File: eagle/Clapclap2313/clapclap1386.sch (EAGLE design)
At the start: 26 parts, among them IC1 TINY13-20PU, J1 AVR_SPI_PRG_6PTH, K1 4052, M1 Mic, U1 LM386

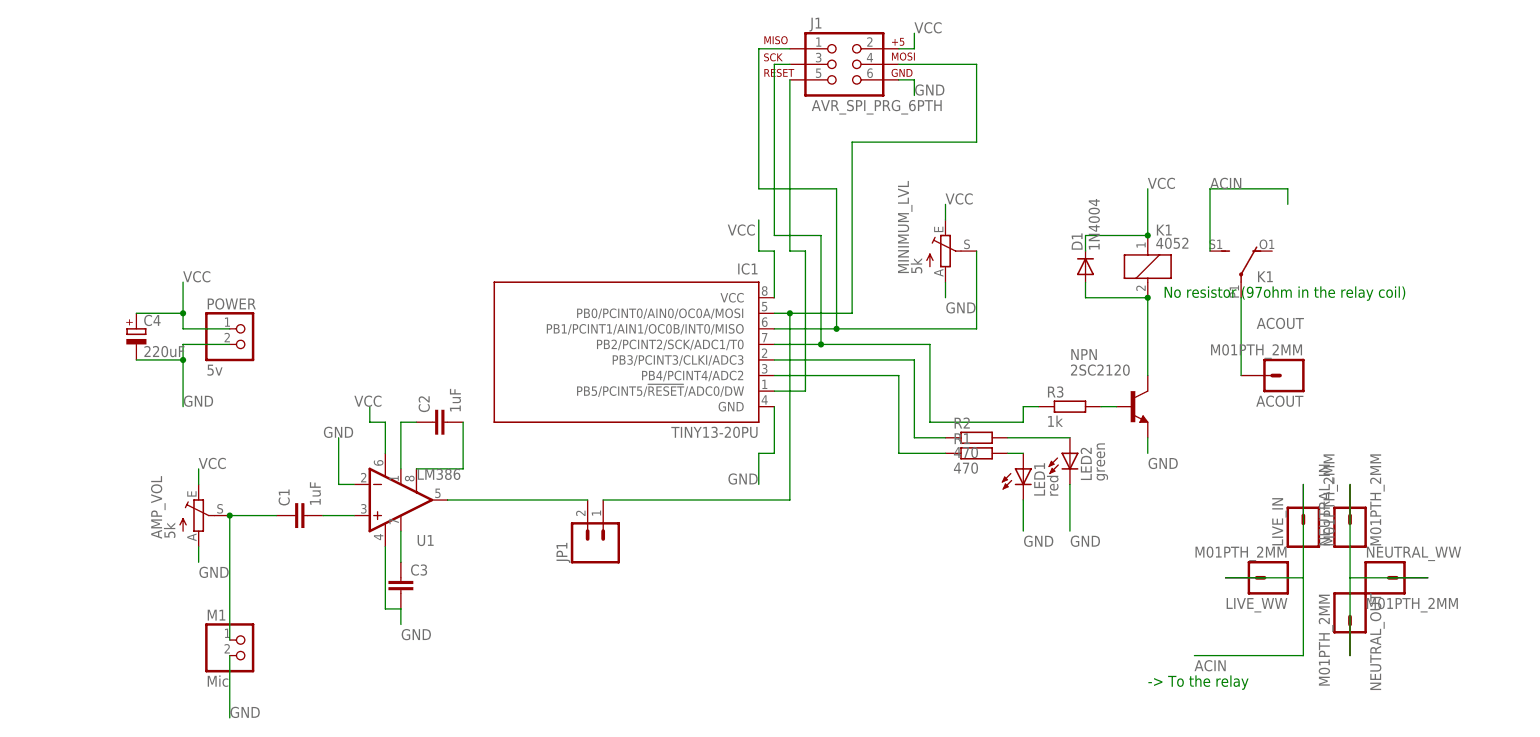
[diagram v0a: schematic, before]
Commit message: Clapclap 1386 Beta version : needs holes and full verification
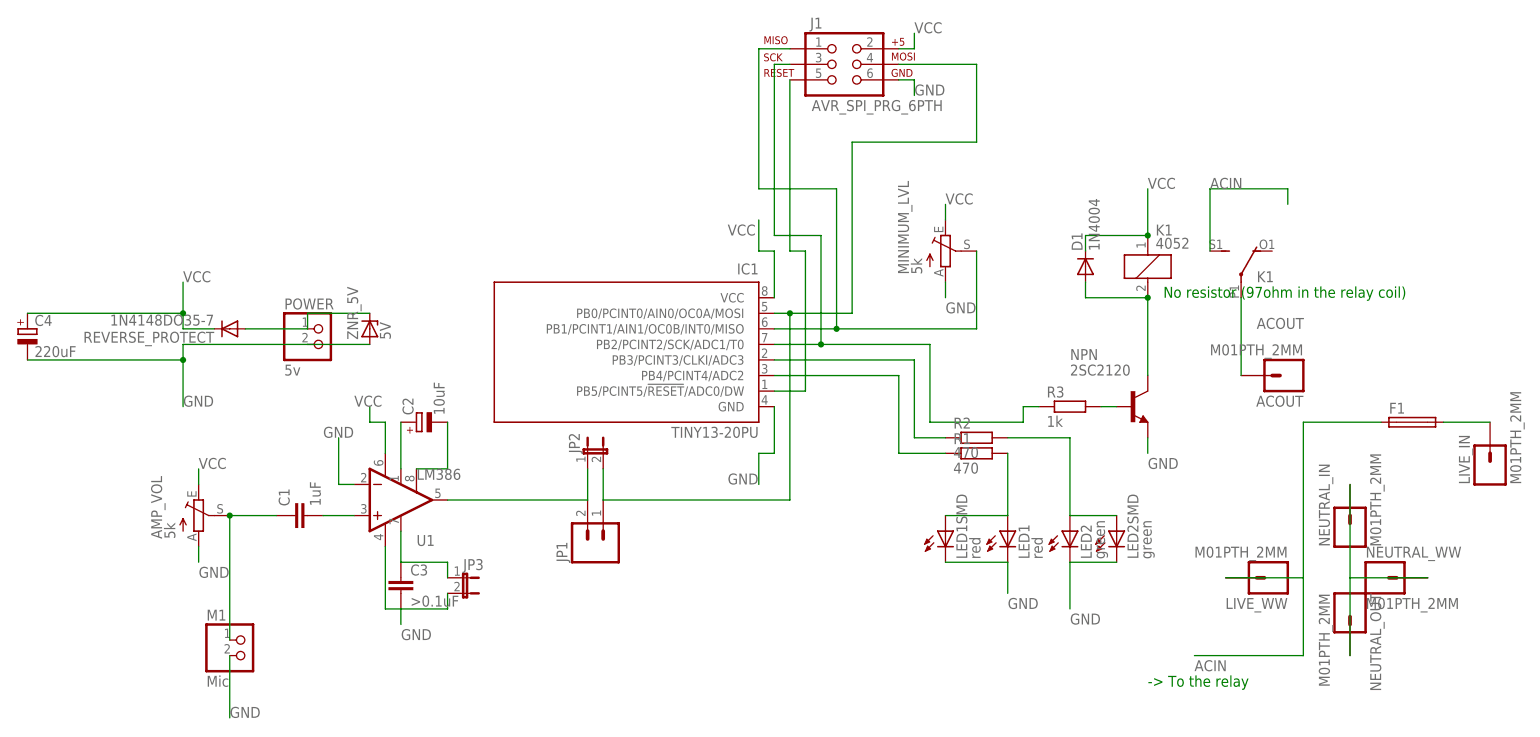
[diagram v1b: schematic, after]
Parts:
- added F1: (no value), fuse:TE5
- added JP2, JP3: (no value), SparkFun-Passives:JUMPER-2SMD-NO
- added LED1SMD: red, led:LEDKA-3528ASYC
- added LED2SMD: green, led:LEDKA-3528ASYC
- added REVERSE_PROTECT: 1N4148DO35-7, diode:1N4148DO35-7
- added ZNR_5V: 5V, diode:ZENER-DIODEZD-2.5
- C2: value 1uF -> 10uF; device resistor:C-EU025-025X050 -> resistor:CPOL-EUE2,5-6E
- C3: value (none) -> >0.1uF
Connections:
- new net N$18: POWER.1, REVERSE_PROTECT.A, ZNR_5V.C
- new net N$19: F1.2, LIVE_IN.1
- net ACIN: now also F1.1; no longer LIVE_IN.1
- net GND: now also JP3.2, LED1SMD.C, LED2SMD.C, ZNR_5V.A
- net N$10: now also JP2.2
- net N$11: now also LED2SMD.A
- net N$14: now also C2.-; no longer C2.2
- net N$15: now also JP3.1
- net N$17: now also JP2.1
- net N$5: now also C2.+; no longer C2.1
- net N$7: now also LED1SMD.A
- net VCC: now also REVERSE_PROTECT.C; no longer POWER.1
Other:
- moved on the sheet: C4, LED1, LED2, LIVE_IN, POWER

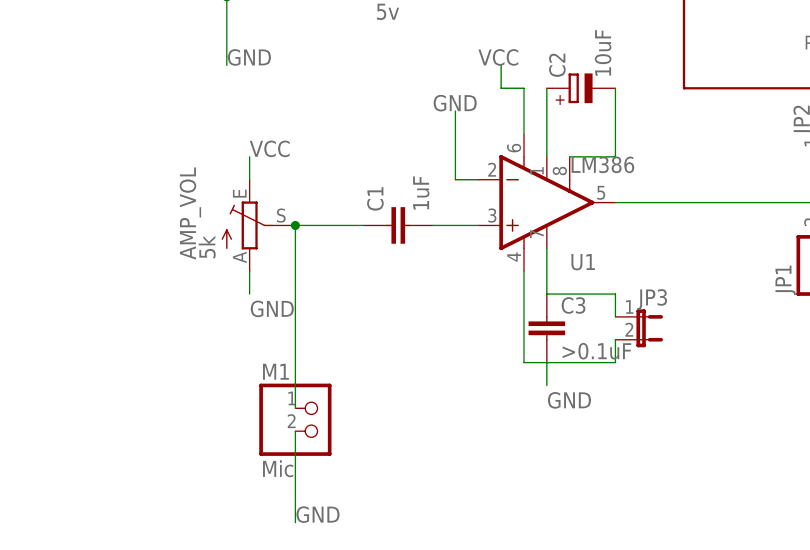
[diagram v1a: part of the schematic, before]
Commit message: Added a jumper to bypass the input+ of the opamp
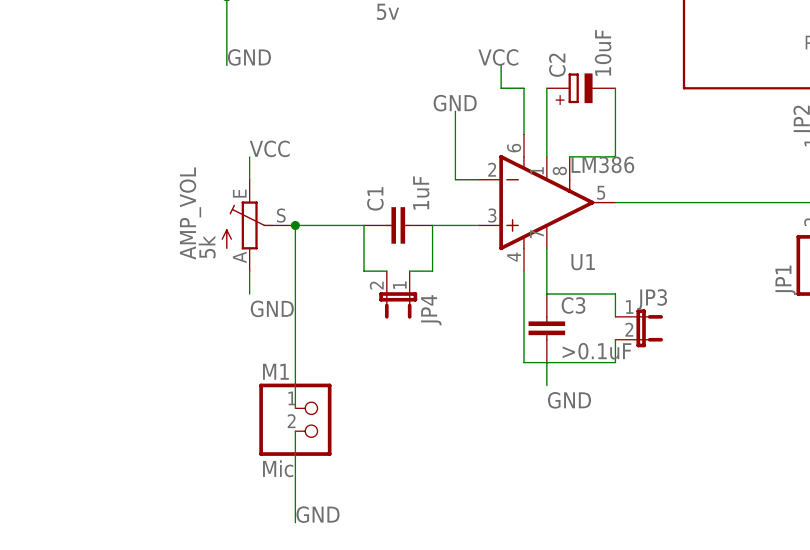
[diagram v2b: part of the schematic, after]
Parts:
- added JP4: (no value), SparkFun-Passives:JUMPER-2SMD-NO
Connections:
- net N$1: now also JP4.1
- net N$3: now also JP4.2
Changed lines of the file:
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@@
 <part name="ZNR_5V" library="diode" deviceset="ZENER-DIODE" device="ZD-2.5" value="5V"/>
 <part name="F1" library="fuse" deviceset="TE5" device=""/>
+<part name="JP4" library="SparkFun-Passives" deviceset="JUMPER-2" device="SMD-NO"/>
 </parts>
 <sheets>
@@
 <instance part="ZNR_5V" gate="G$1" x="-17.78" y="76.2" rot="R90"/>
 <instance part="F1" gate="1" x="152.4" y="60.96"/>
+<instance part="JP4" gate="A" x="-27.94" y="38.1" rot="R180"/>
 </instances>
 <busses>
@@
 <pinref part="C1" gate="G$1" pin="1"/>
 <pinref part="M1" gate="G$1" pin="1"/>
+<wire x1="-30.48" y1="40.64" x2="-33.02" y2="40.64" width="0.1524" layer="91"/>
+<wire x1="-33.02" y1="40.64" x2="-33.02" y2="45.72" width="0.1524" layer="91"/>
+<pinref part="JP4" gate="A" pin="2"/>
 </segment>
 </net>
@@
 <pinref part="U1" gate="G$1" pin="+IN"/>
 <wire x1="-25.4" y1="45.72" x2="-20.32" y2="45.72" width="0.1524" layer="91"/>
-</segment>
-</net>
+<wire x1="-25.4" y1="45.72" x2="-25.4" y2="40.64" width="0.1524" layer="91"/>
+<pinref part="JP4" gate="A" pin="1"/>
+<wire x1="-25.4" y1="40.64" x2="-27.94" y2="40.64" width="0.1524" layer="91"/>
+</segment>
+</net>

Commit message: v1.0 sent to production in HK.
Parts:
- removed JP4: (no value), SparkFun-Passives:JUMPER-2SMD-NO
- added JP5, JP7, JP8: (no value), SparkFun-Passives:JUMPER-2SMD-NO
- added JP6, JP9: (no value), SparkFun-Connectors:M02PTH
- C2: value 10uF -> >=1uF; device resistor:CPOL-EUE2,5-6E -> resistor:C-EU050-024X044
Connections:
- removed net N$2: IC1.PB2/PCINT2/SCK/ADC1/T0, J1.3, R3.1
- new net N$21: JP6.1, JP7.2, MINIMUM_LVL.S
- new net N$23: IC1.PB2/PCINT2/SCK/ADC1/T0, J1.3, JP8.1, JP9.2
- new net N$24: JP8.2, JP9.1, R3.1
- net N$1: no longer JP4.1
- net N$12: now also JP6.2, JP7.1; no longer MINIMUM_LVL.S
- net N$14: now also C2.2, JP5.2; no longer C2.-
- net N$3: no longer JP4.2
- net N$5: now also C2.1, JP5.1; no longer C2.+
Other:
- note added: "Bypass cap (leave open or big cap, grounding shift output to 0v center)"
- note added: "Gain cap (optional, if present better gain else default 20x)"
- note added: "Input cap (mandatory)"
- moved on the sheet: C4, MINIMUM_LVL, POWER, REVERSE_PROTECT, ZNR_5V
